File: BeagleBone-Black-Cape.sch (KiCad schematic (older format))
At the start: 2 parts, among them P101 BeagleBone_Black_Header, P102 BeagleBone_Black_Header

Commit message: Added Footprints for UI, JTAG, and some power stuff.
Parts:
- renumbered P101 to P?, P102 to P?
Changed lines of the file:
@@
 Connection ~ 4450 4700
 $Comp
-L BeagleBone-Black-Cape-rescue:+3.3V-power #PWR0106
+L BeagleBone-Black-Cape-rescue:+3.3V-power #PWR0101
 U 1 1 55897A67
 P 4450 2300
-F 0 "#PWR0106" H 4450 2150 50  0001 C CNN
+F 0 "#PWR0101" H 4450 2150 50  0001 C CNN
 F 1 "+3V3" H 4450 2440 50  0000 C CNN
 F 2 "" H 4450 2300 60  0000 C CNN
@@
 $EndComp
 $Comp
-L BeagleBone-Black-Cape-rescue:+5V-power #PWR0107
+L BeagleBone-Black-Cape-rescue:+5V-power #PWR0102
 U 1 1 55897A7F
 P 4650 2300
-F 0 "#PWR0107" H 4650 2150 50  0001 C CNN
+F 0 "#PWR0102" H 4650 2150 50  0001 C CNN
 F 1 "+5V" H 4650 2440 50  0000 C CNN
 F 2 "" H 4650 2300 60  0000 C CNN
@@
 	4900 2800 4300 2800
 $Comp
-L BeagleBone-Black-Cape-rescue:+3.3V-power #PWR0104
+L BeagleBone-Black-Cape-rescue:+3.3V-power #PWR0103
 U 1 1 55897EE7
 P 3650 2300
-F 0 "#PWR0104" H 3650 2150 50  0001 C CNN
+F 0 "#PWR0103" H 3650 2150 50  0001 C CNN
 F 1 "+3V3" H 3650 2440 50  0000 C CNN
 F 2 "" H 3650 2300 60  0000 C CNN
@@
 $EndComp
 $Comp
-L BeagleBone-Black-Cape-rescue:+5V-power #PWR0103
+L BeagleBone-Black-Cape-rescue:+5V-power #PWR0104
 U 1 1 55897EF8
 P 3450 2300
-F 0 "#PWR0103" H 3450 2150 50  0001 C CNN
+F 0 "#PWR0104" H 3450 2150 50  0001 C CNN
 F 1 "+5V" H 3450 2440 50  0000 C CNN
 F 2 "" H 3450 2300 60  0000 C CNN
@@
 	6500 2500 6750 2500
 $Comp
-L pwr_BeagleBone:SYS_5V #PWR0110
+L pwr_BeagleBone:SYS_5V #PWR0105
 U 1 1 55898497
 P 4900 2300
-F 0 "#PWR0110" H 4900 2150 50  0001 C CNN
+F 0 "#PWR0105" H 4900 2150 50  0001 C CNN
 F 1 "SYS_5V" H 4900 2440 50  0000 C CNN
 F 2 "" H 4900 2300 60  0000 C CNN
@@
 $EndComp
 $Comp
-L pwr_BeagleBone:SYS_5V #PWR0102
+L pwr_BeagleBone:SYS_5V #PWR0106
 U 1 1 558984AF
 P 3200 2300
-F 0 "#PWR0102" H 3200 2150 50  0001 C CNN
+F 0 "#PWR0106" H 3200 2150 50  0001 C CNN
 F 1 "SYS_5V" H 3200 2440 50  0000 C CNN
 F 2 "" H 3200 2300 60  0000 C CNN
@@
 	3800 2900 3700 2900
 $Comp
-L BeagleBone-Black-Cape-rescue:Conn_02x23_Odd_Even-Connector_Generic P101
+L BeagleBone-Black-Cape-rescue:Conn_02x23_Odd_Even-Connector_Generic P?
 U 1 1 55DF7DBA
 P 4000 3600
-F 0 "P101" H 4000 4800 50  0000 C CNN
+F 0 "P?" H 4000 4800 50  0000 C CNN
 F 1 "BeagleBone_Black_Header" V 4050 3650 50  0000 C CNN
 F 2 "Socket_BeagleBone_Black:Socket_BeagleBone_Black" H 4000 2750 60  0001 C CNN
@@
 $EndComp
 $Comp
-L BeagleBone-Black-Cape-rescue:Conn_02x23_Odd_Even-Connector_Generic P102
+L BeagleBone-Black-Cape-rescue:Conn_02x23_Odd_Even-Connector_Generic P?
 U 1 1 55DF7DE1
 P 6200 3600
-F 0 "P102" H 6200 4800 50  0000 C CNN
+F 0 "P?" H 6200 4800 50  0000 C CNN
 F 1 "BeagleBone_Black_Header" V 6250 3650 50  0000 C CNN
 F 2 "Socket_BeagleBone_Black:Socket_BeagleBone_Black" H 6200 2750 60  0001 C CNN
@@
 	3600 3200 3800 3200
 $Sheet
-S 12450 12300 8350 4400
+S 12400 12450 8350 4400
 U 60837686
 F0 "UI_subsystem" 50
@@
 	3650 4900 4050 4900
 $Comp
-L power:GND #PWR?
+L power:GND #PWR0107
 U 1 1 614B4DBF
 P 4050 4900
-F 0 "#PWR?" H 4050 4650 50  0001 C CNN
+F 0 "#PWR0107" H 4050 4650 50  0001 C CNN
 F 1 "GND" H 4055 4727 50  0000 C CNN
 F 2 "" H 4050 4900 50  0001 C CNN
@@
 	4050 4900 4450 4900
 $Comp
-L power:GND #PWR?
+L power:GND #PWR0108
 U 1 1 614B5823
 P 5100 2500
-F 0 "#PWR?" H 5100 2250 50  0001 C CNN
+F 0 "#PWR0108" H 5100 2250 50  0001 C CNN
 F 1 "GND" H 5105 2327 50  0000 C CNN
 F 2 "" H 5100 2500 50  0001 C CNN
@@
 $EndComp
 $Comp
-L power:GND #PWR?
+L power:GND #PWR0109
 U 1 1 614B6213
 P 3000 2500
-F 0 "#PWR?" H 3000 2250 50  0001 C CNN
+F 0 "#PWR0109" H 3000 2250 50  0001 C CNN
 F 1 "GND" H 3005 2327 50  0000 C CNN
 F 2 "" H 3000 2500 50  0001 C CNN
@@
 $EndComp
 $Comp
-L power:GND #PWR?
+L power:GND #PWR0110
 U 1 1 614B8C07
 P 5750 2500
-F 0 "#PWR?" H 5750 2250 50  0001 C CNN
+F 0 "#PWR0110" H 5750 2250 50  0001 C CNN
 F 1 "GND" H 5755 2327 50  0000 C CNN
 F 2 "" H 5750 2500 50  0001 C CNN
@@
 $EndComp
 $Comp
-L power:GND #PWR?
+L power:GND #PWR0111
 U 1 1 614B962C
 P 6750 2500
-F 0 "#PWR?" H 6750 2250 50  0001 C CNN
+F 0 "#PWR0111" H 6750 2250 50  0001 C CNN
 F 1 "GND" H 6755 2327 50  0000 C CNN
 F 2 "" H 6750 2500 50  0001 C CNN

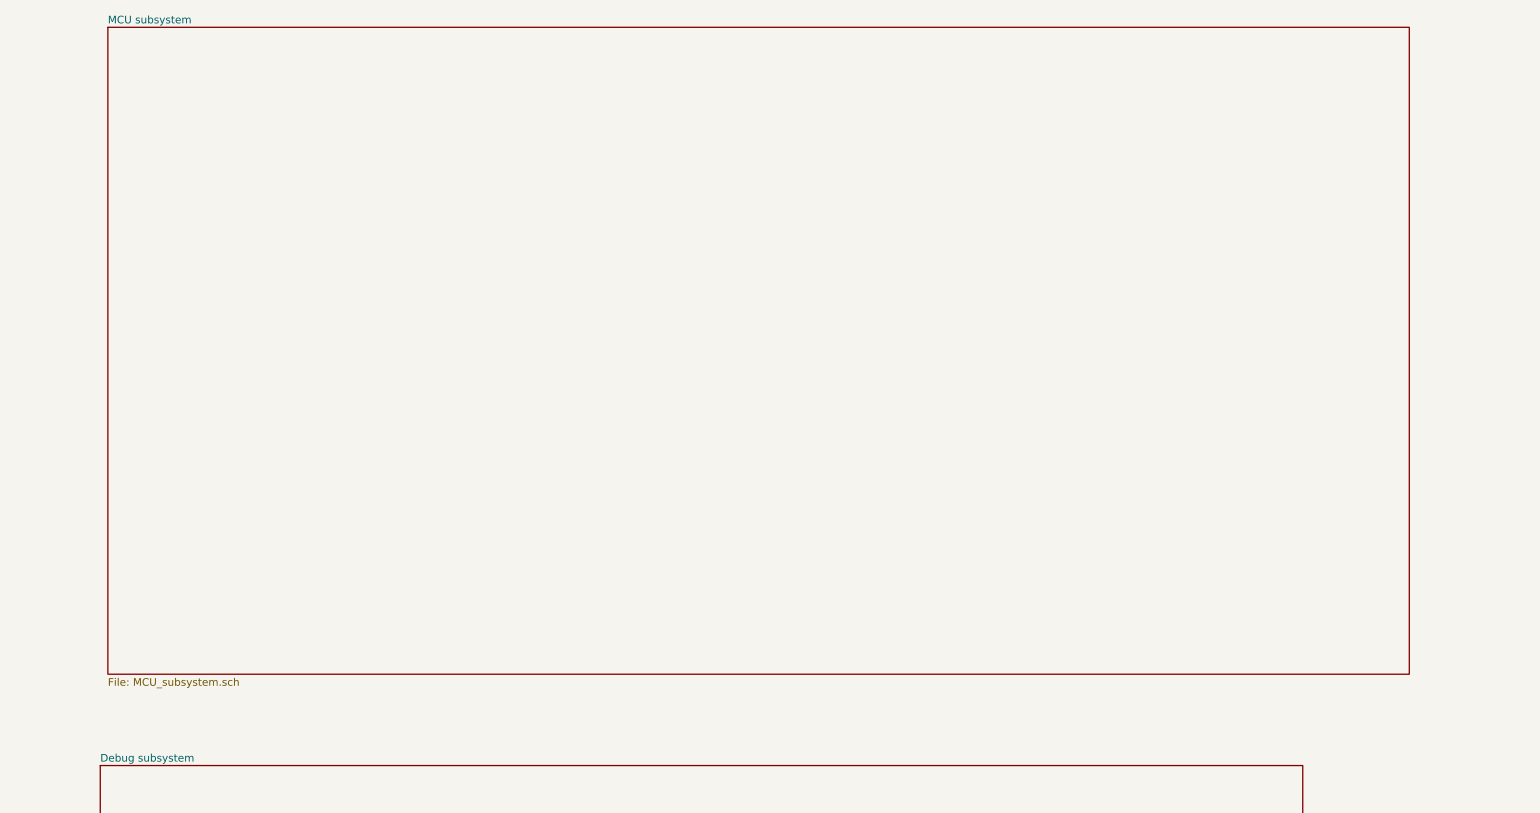
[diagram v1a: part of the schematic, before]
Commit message: Added Flash IC and PB/LED footprints.
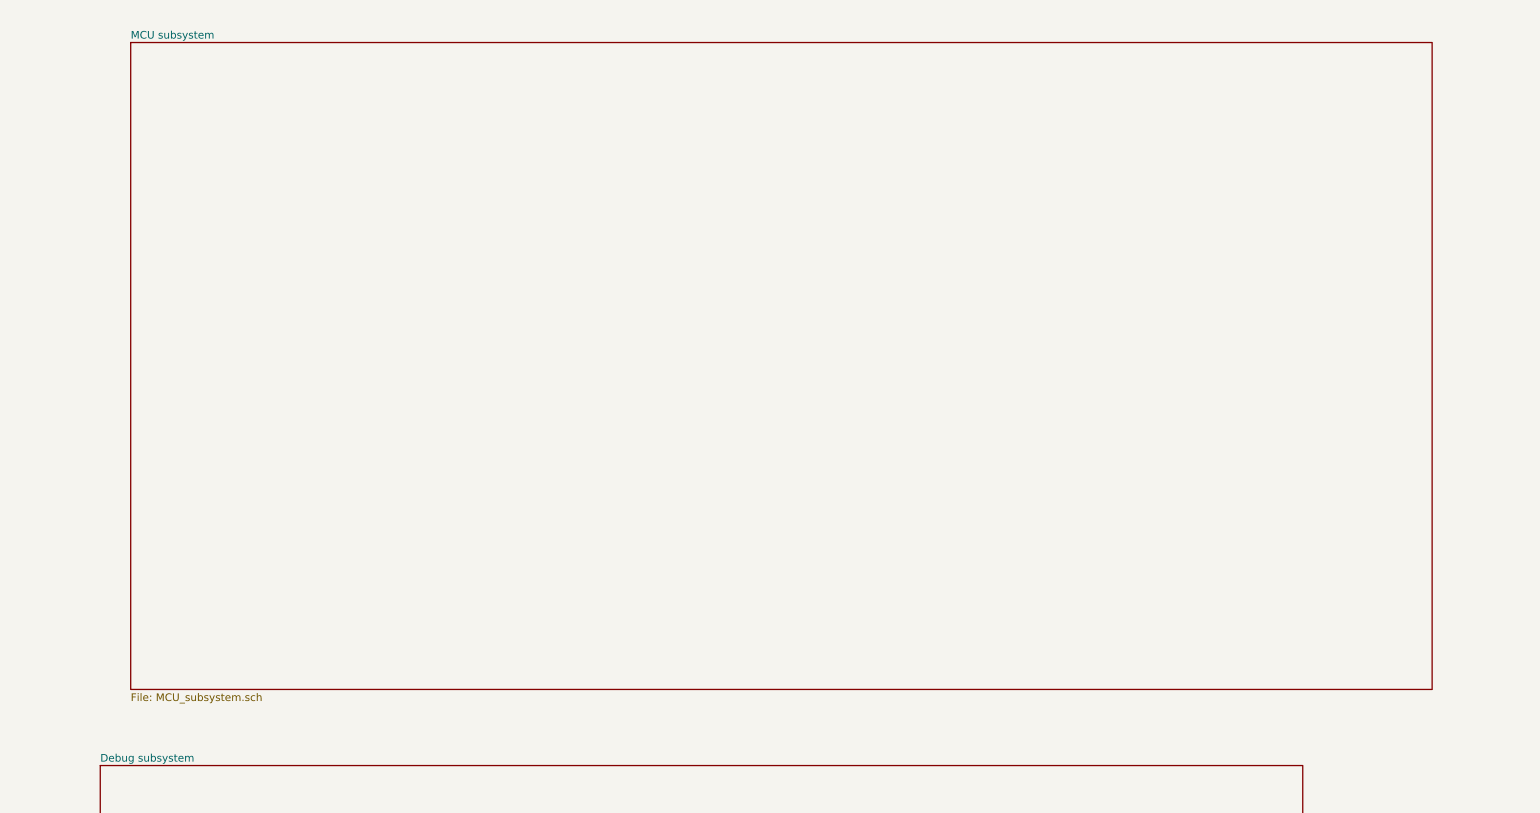
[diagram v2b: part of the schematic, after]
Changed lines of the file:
@@
 $EndComp
 $Sheet
-S 12900 -7450 8550 4250
+S 13050 -7350 8550 4250
 U 614C2CA1
 F0 "MCU subsystem" 50

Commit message: This is a new commit.
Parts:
- gave numbers to parts that had none: 2
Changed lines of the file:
@@
 	3800 2900 3700 2900
 $Comp
-L BeagleBone-Black-Cape-rescue:Conn_02x23_Odd_Even-Connector_Generic P?
+L BeagleBone-Black-Cape-rescue:Conn_02x23_Odd_Even-Connector_Generic P1
 U 1 1 55DF7DBA
 P 4000 3600
-F 0 "P?" H 4000 4800 50  0000 C CNN
+F 0 "P1" H 4000 4800 50  0000 C CNN
 F 1 "BeagleBone_Black_Header" V 4050 3650 50  0000 C CNN
 F 2 "Socket_BeagleBone_Black:Socket_BeagleBone_Black" H 4000 2750 60  0001 C CNN
@@
 $EndComp
 $Comp
-L BeagleBone-Black-Cape-rescue:Conn_02x23_Odd_Even-Connector_Generic P?
+L BeagleBone-Black-Cape-rescue:Conn_02x23_Odd_Even-Connector_Generic P2
 U 1 1 55DF7DE1
 P 6200 3600
-F 0 "P?" H 6200 4800 50  0000 C CNN
+F 0 "P2" H 6200 4800 50  0000 C CNN
 F 1 "BeagleBone_Black_Header" V 6250 3650 50  0000 C CNN
 F 2 "Socket_BeagleBone_Black:Socket_BeagleBone_Black" H 6200 2750 60  0001 C CNN
